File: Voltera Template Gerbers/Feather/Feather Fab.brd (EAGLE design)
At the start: 101.6 x 76.2 mm, 1 part

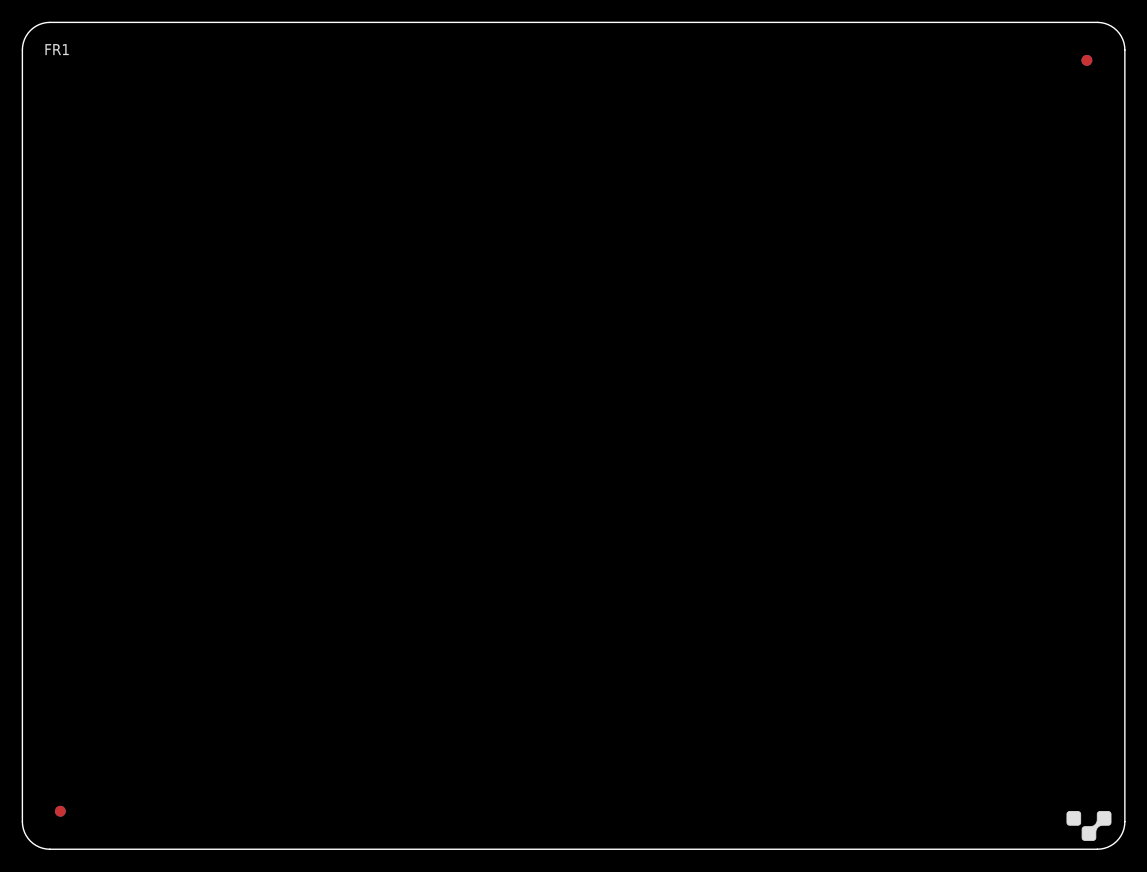
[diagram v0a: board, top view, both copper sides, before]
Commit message: Added Feather board, updated community library and added substrate gerbers
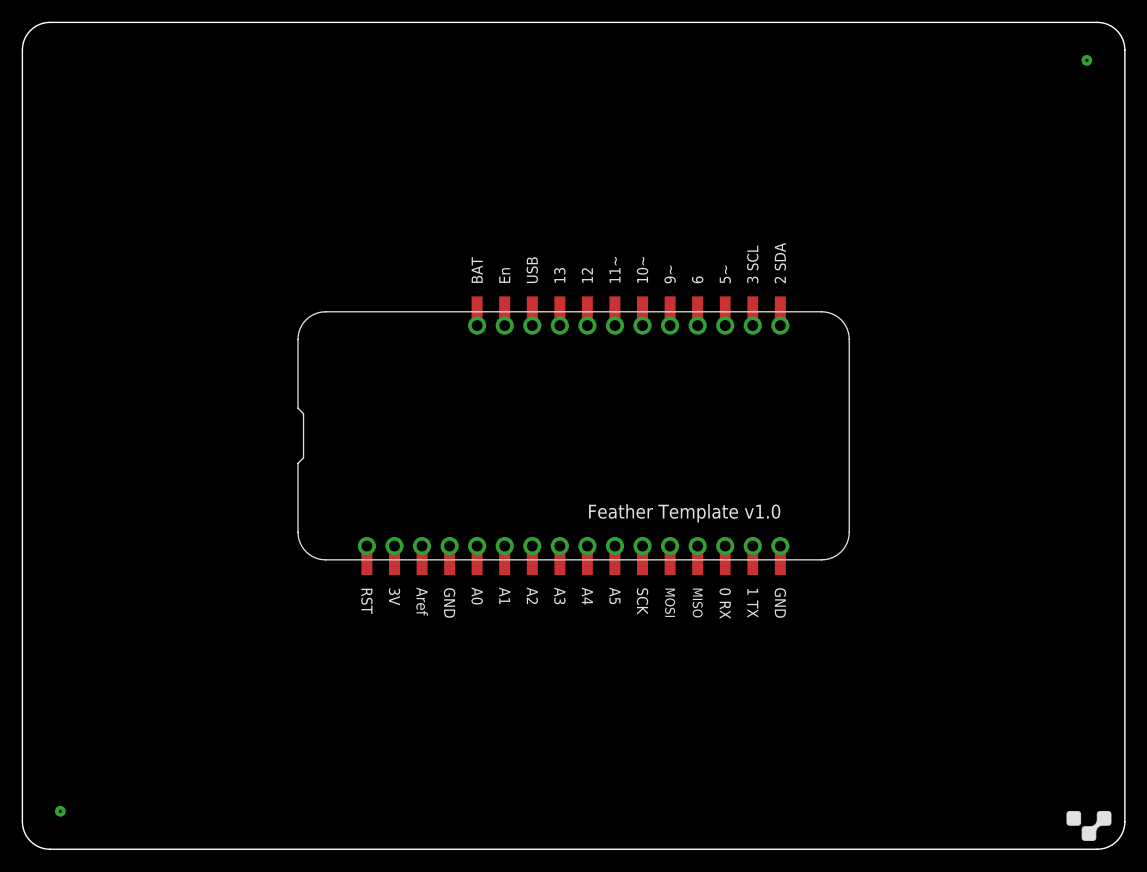
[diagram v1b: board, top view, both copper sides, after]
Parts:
- E$1: device voltera_EAGLE_community_lib:3X4_BOARD_FR1 -> voltera_EAGLE_community_lib:FEATHER_FAB
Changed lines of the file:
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@@
 <?xml version="1.0" encoding="utf-8"?>
 <!DOCTYPE eagle SYSTEM "eagle.dtd">
-<eagle version="6.6.0">
+<eagle version="9.0.1">
 <drawing>
 <settings>
@@
 <setting verticaltext="up"/>
 </settings>
-<grid distance="0.05" unitdist="inch" unit="inch" style="lines" multiple="1" display="no" altdistance="0.025" altunitdist="inch" altunit="inch"/>
+<grid distance="50" unitdist="mil" unit="mil" style="lines" multiple="1" display="no" altdistance="5" altunitdist="mil" altunit="mil"/>
 <layers>
 <layer number="1" name="Top" color="4" fill="1" visible="yes" active="yes"/>
 <layer number="2" name="Route2" color="1" fill="3" visible="no" active="no"/>
-<layer number="3" name="Route3" color="4" fill="3" visible="no" active="no"/>
-<layer number="4" name="Route4" color="1" fill="4" visible="no" active="no"/>
-<layer number="5" name="Route5" color="4" fill="4" visible="no" active="no"/>
-<layer number="6" name="Route6" color="1" fill="8" visible="no" active="no"/>
-<layer number="7" name="Route7" color="4" fill="8" visible="no" active="no"/>
-<layer number="8" name="Route8" color="1" fill="2" visible="no" active="no"/>
-<layer number="9" name="Route9" color="4" fill="2" visible="no" active="no"/>
-<layer number="10" name="Route10" color="1" fill="7" visible="no" active="no"/>
-<layer number="11" name="Route11" color="4" fill="7" visible="no" active="no"/>
-<layer number="12" name="Route12" color="1" fill="5" visible="no" active="no"/>
-<layer number="13" name="Route13" color="4" fill="5" visible="no" active="no"/>
-<layer number="14" name="Route14" color="1" fill="6" visible="no" active="no"/>
 <layer number="15" name="Route15" color="4" fill="6" visible="no" active="no"/>
 <layer number="16" name="Bottom" color="1" fill="1" visible="yes" active="yes"/>
@@
 <layer number="18" name="Vias" color="2" fill="1" visible="yes" active="yes"/>
 <layer number="19" name="Unrouted" color="6" fill="1" visible="yes" active="yes"/>
-<layer number="20" name="Dimension" color="15" fill="1" visible="yes" active="yes"/>
+<layer number="20" name="Dimension" color="24" fill="1" visible="yes" active="yes"/>
 <layer number="21" name="tPlace" color="7" fill="1" visible="yes" active="yes"/>
 <layer number="22" name="bPlace" color="7" fill="1" visible="yes" active="yes"/>
@@
 <layer number="223" name="223bmp" color="24" fill="1" visible="no" active="no"/>
 <layer number="224" name="224bmp" color="25" fill="1" visible="no" active="no"/>
+<layer number="225" name="225bmp" color="7" fill="1" visible="yes" active="yes"/>
+<layer number="226" name="226bmp" color="7" fill="1" visible="yes" active="yes"/>
+<layer number="227" name="227bmp" color="7" fill="1" visible="yes" active="yes"/>
+<layer number="228" name="228bmp" color="7" fill="1" visible="yes" active="yes"/>
+<layer number="229" name="229bmp" color="7" fill="1" visible="yes" active="yes"/>
+<layer number="230" name="230bmp" color="7" fill="1" visible="yes" active="yes"/>
 <layer number="231" name="Eagle3D_PG1" color="7" fill="1" visible="no" active="no"/>
 <layer number="232" name="Eagle3D_PG2" color="7" fill="1" visible="no" active="no"/>
@@
 <layer number="251" name="SMDround" color="12" fill="11" visible="no" active="no"/>
 <layer number="254" name="cooling" color="7" fill="1" visible="yes" active="yes"/>
+<layer number="255" name="routoute" color="7" fill="1" visible="yes" active="yes"/>
 </layers>
 <board>
@@
 <param name="mtCopper" value="0.035mm 0.035mm 0.035mm 0.035mm 0.035mm 0.035mm 0.035mm 0.035mm 0.035mm 0.035mm 0.035mm 0.035mm 0.035mm 0.035mm 0.035mm 0.035mm"/>
 <param name="mtIsolate" value="1.5mm 0.15mm 0.2mm 0.15mm 0.2mm 0.15mm 0.2mm 0.15mm 0.2mm 0.15mm 0.2mm 0.15mm 0.2mm 0.15mm 0.2mm"/>
-<param name="mdWireWire" value="8mil"/>
-<param name="mdWirePad" value="8mil"/>
-<param name="mdWireVia" value="8mil"/>
-<param name="mdPadPad" value="8mil"/>
-<param name="mdPadVia" value="8mil"/>
-<param name="mdViaVia" value="8mil"/>
-<param name="mdSmdPad" value="8mil"/>
-<param name="mdSmdVia" value="8mil"/>
-<param name="mdSmdSmd" value="8mil"/>
-<param name="mdViaViaSameLayer" value="8mil"/>
+<param name="mdWireWire" value="6mil"/>
+<param name="mdWirePad" value="6mil"/>
+<param name="mdWireVia" value="6mil"/>
+<param name="mdPadPad" value="6mil"/>
+<param name="mdPadVia" value="6mil"/>
+<param name="mdViaVia" value="6mil"/>
+<param name="mdSmdPad" value="6mil"/>
+<param name="mdSmdVia" value="6mil"/>
+<param name="mdSmdSmd" value="6mil"/>
+<param name="mdViaViaSameLayer" value="6mil"/>
 <param name="mnLayersViaInSmd" value="2"/>
 <param name="mdCopperDimension" value="40mil"/>
-<param name="mdDrill" value="8mil"/>
+<param name="mdDrill" value="6mil"/>
 <param name="mdSmdStop" value="0mil"/>
-<param name="msWidth" value="10mil"/>
-<param name="msDrill" value="24mil"/>
+<param name="msWidth" value="6mil"/>
+<param name="msDrill" value="0.35mm"/>
 <param name="msMicroVia" value="9.99mm"/>
 <param name="msBlindViaRatio" value="0.5"/>
@@
 <param name="dpMaxLengthDifference" value="10mm"/>
 <param name="dpGapFactor" value="2.5"/>
-<param name="checkGrid" value="0"/>
 <param name="checkAngle" value="0"/>
 <param name="checkFont" value="1"/>
 <param name="checkRestrict" value="1"/>
+<param name="checkStop" value="0"/>
+<param name="checkValues" value="0"/>
 <param name="useDiameter" value="13"/>
 <param name="maxErrors" value="50"/>
@@
 <pass name="Default">
 <param name="RoutingGrid" value="50mil"/>
+<param name="AutoGrid" value="1"/>
+<param name="Efforts" value="0"/>
+<param name="TopRouterVariant" value="1"/>
 <param name="tpViaShape" value="round"/>
-<param name="PrefDir.1" value="|"/>
+<param name="PrefDir.1" value="a"/>
 <param name="PrefDir.2" value="0"/>
 <param name="PrefDir.3" value="0"/>
@@
 <param name="PrefDir.14" value="0"/>
 <param name="PrefDir.15" value="0"/>
-<param name="PrefDir.16" value="-"/>
+<param name="PrefDir.16" value="a"/>
 <param name="cfVia" value="8"/>
 <param name="cfNonPref" value="5"/>
@@
 </autorouter>
 <elements>
-<element name="E$1" library="voltera_EAGLE_community_lib" package="3X4_BOARD_FR1" value="" x="0" y="0"/>
+<element name="E$1" library="voltera_EAGLE_community_lib" package="FEATHER_FAB" value="" x="0" y="0"/>
 </elements>
 <signals>
